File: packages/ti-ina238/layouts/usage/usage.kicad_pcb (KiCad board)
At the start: 2 copper layers, 5 parts

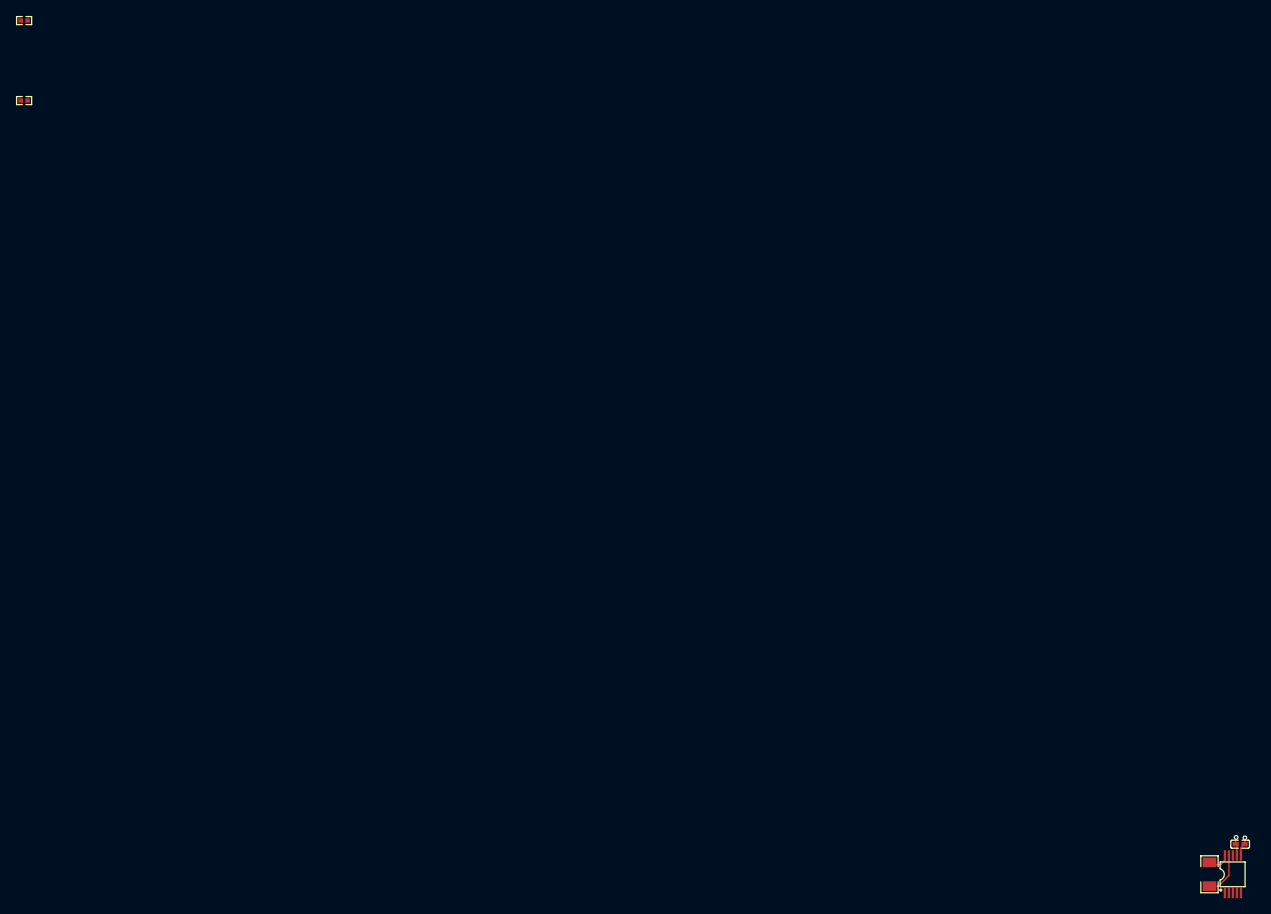
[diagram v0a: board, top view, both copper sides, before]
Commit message: multipackage: Run builds with latest compiler to fix frozen errors (#183)
* fix rohm-bh1750

* fix rj45-connectors

* fix sensirion-scd40

* fix sensirion-scd41

* update package versions for release

* sensirion-sgp40: LLM Update with 0.12.4

Updated sensirion-sgp40 package to work with atopile compiler version 0.12.4.

Changes made:
- Updated requires-atopile from ^0.10.8 to ^0.12.4
- Updated package version from 0.1.0 to 0.1.1
- Rebuilt layouts with new compiler (net naming improvements)
- All builds pass: ato build, ato build --frozen, ato package verify -s

🤖 Generated with [Claude Code](https://claude.ai/code)

Co-Authored-By: Claude <noreply@anthropic.com>

* sensirion-sht31: LLM Update with 0.12.4

Updated sensirion-sht31 package to work with atopile compiler version 0.12.4.

Changes made:
- Updated requires-atopile from ^0.10.8 to ^0.12.4
- Updated package version from 0.1.0 to 0.1.1
- Rebuilt layouts with new compiler (net naming improvements)
- All builds pass: ato build, ato build --frozen, ato package verify -s

🤖 Generated with [Claude Code](https://claude.ai/code)

Co-Authored-By: Claude <noreply@anthropic.com>

* sensirion-sht40: LLM Update with 0.12.4

Updated sensirion-sht40 package to work with atopile compiler version 0.12.4.

Changes made:
- Updated requires-atopile from ^0.10.8 to ^0.12.4
- Updated package version from 0.1.0 to 0.1.1
- Rebuilt layouts with new compiler (net naming improvements)
- All builds pass: ato build, ato build --frozen, ato package verify -s

🤖 Generated with [Claude Code](https://claude.ai/code)

Co-Authored-By: Claude <noreply@anthropic.com>

* sensirion-sht41: LLM Update with 0.12.4

Updated sensirion-sht41 package to work with atopile compiler version 0.12.4.

Changes made:
- Updated requires-atopile from ^0.10.8 to ^0.12.4
- Updated package version from 0.1.0 to 0.1.1
- Rebuilt layouts with new compiler (net naming improvements)
- All builds pass: ato build, ato build --frozen, ato package verify -s

🤖 Generated wit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
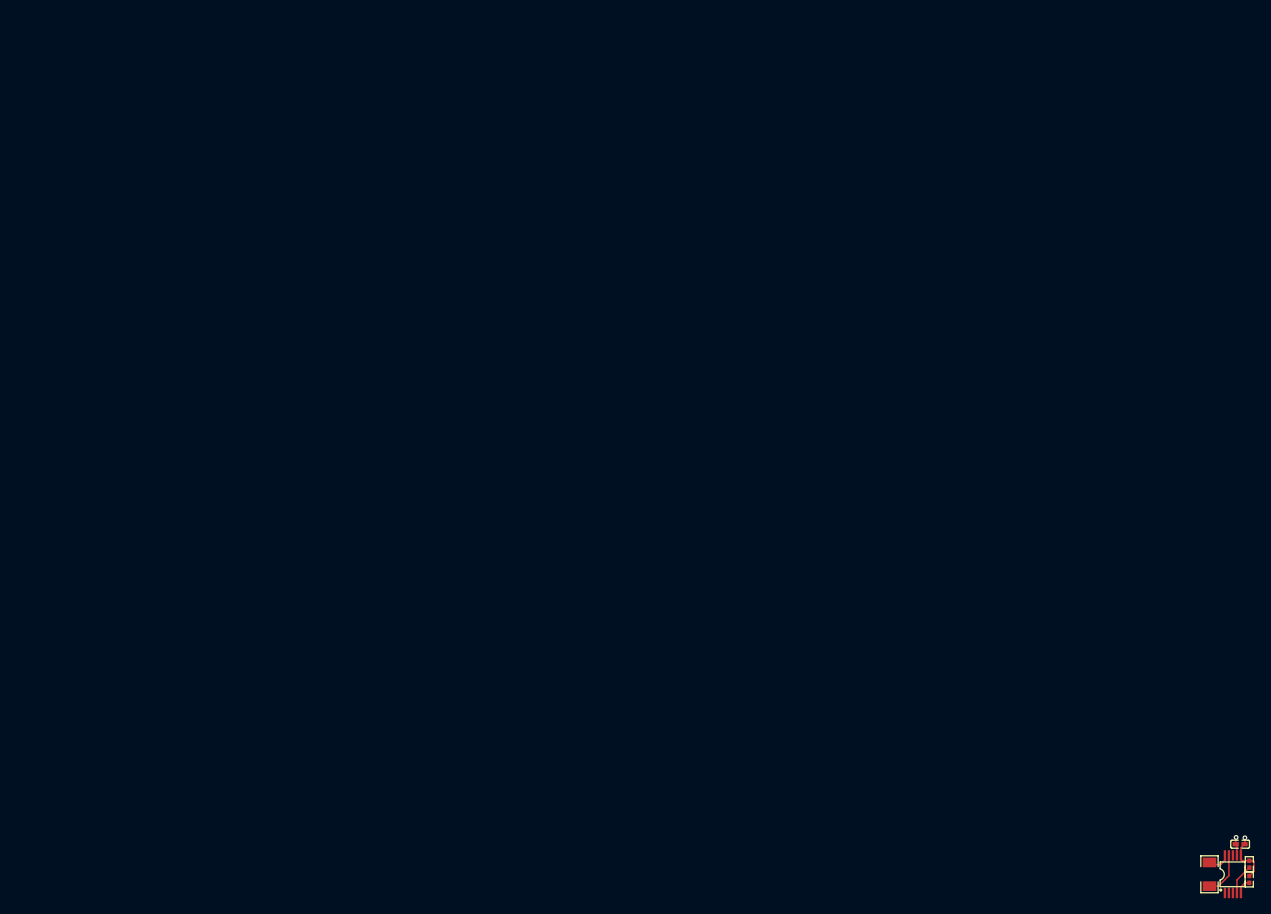
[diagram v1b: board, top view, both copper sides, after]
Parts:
- R1: value 15mΩ ±1% 250mW -> 16mΩ ±1% 1W; footprint Milliohm_HoRF1206_1_4W_15mR_1:R1206 -> Walter_Elec_STE1206M1W0R016F:R1206
- moved R3 185.9 mm to (153.2, 95.5), turned to 90 degrees
- moved R2 181.5 mm to (153.2, 97.3), turned to 90 degrees
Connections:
- net A0 renamed address_bit_0
- net A1 renamed address_bit_1
- net INneg renamed power_out-VCC
- net gnd renamed GND
- net hv renamed power_in-VCC
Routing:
- net power_in-VCC: track 0.00 -> 9.54 mm, vias 0 -> 1
- net (no net): track 5.28 -> 0.00 mm, vias 1 -> 0
- net SDA: track 0.00 -> 3.81 mm
- net SCL: track 0.00 -> 2.02 mm
